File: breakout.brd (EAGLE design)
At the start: 39.4 x 50 mm, 36 parts, among them U1 ATMEGA128RFA1, U2 FT232RL

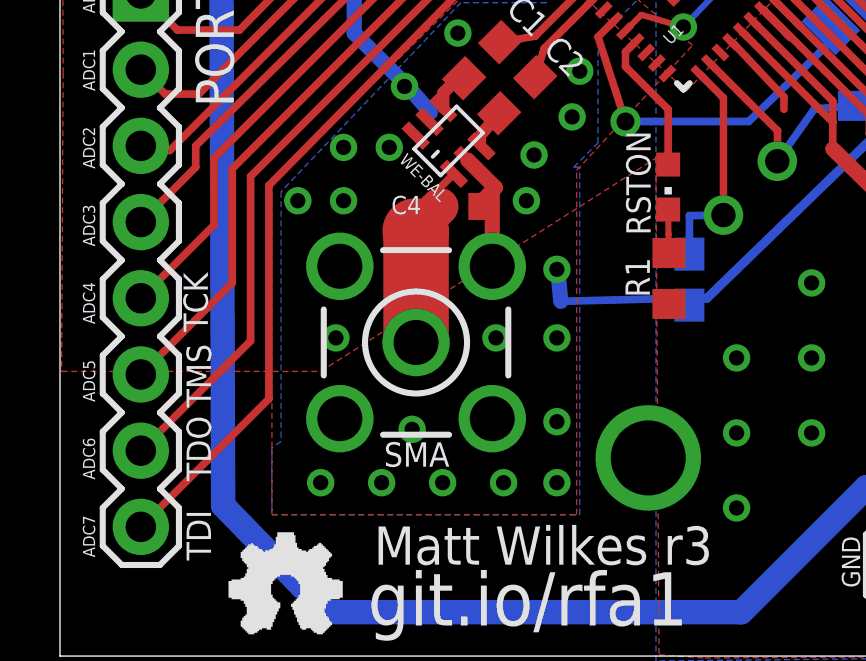
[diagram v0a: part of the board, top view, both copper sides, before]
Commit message: Switch to using a u.fl connector from SMA
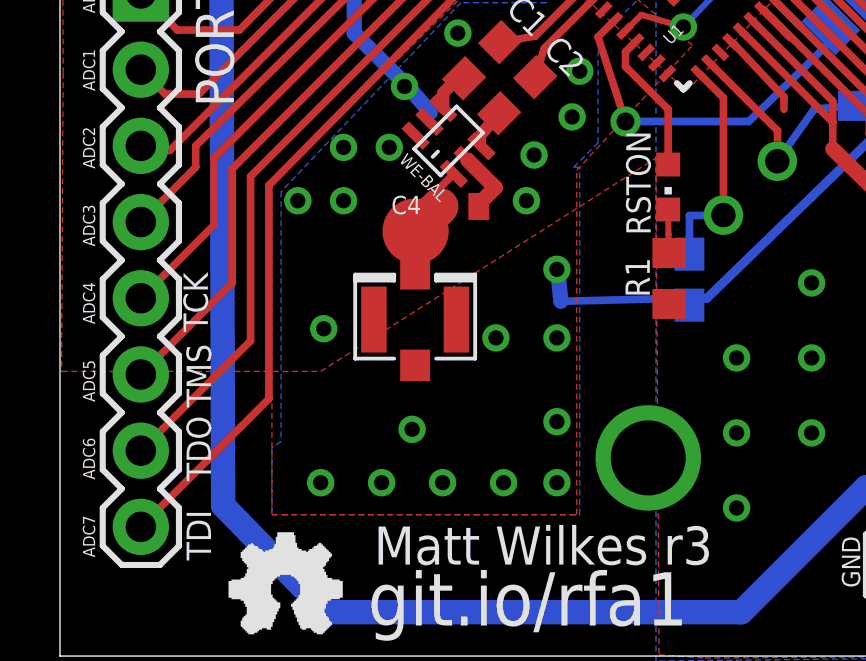
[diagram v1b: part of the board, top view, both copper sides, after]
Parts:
- removed SMA: (no value), con-coax:LTI-SASF54GT
- added U$6: U.FL, SparkFun-Connectors:U.FL
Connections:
- net GNDA: now also U$6.P$1, U$6.P$2; no longer SMA.2, SMA.3, SMA.4, SMA.5
- net SMA: now also U$6.P$3; no longer SMA.1
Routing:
- net SMA: track 6.19 -> 2.48 mm
- net GNDA: track 111.0 -> 108.5 mm
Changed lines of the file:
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@@
 <layer number="106" name="bPlate" color="7" fill="1" visible="no" active="yes"/>
 <layer number="107" name="Crop" color="7" fill="1" visible="no" active="yes"/>
+<layer number="116" name="Patch_BOT" color="9" fill="4" visible="no" active="yes"/>
 <layer number="121" name="_tsilk" color="7" fill="1" visible="no" active="yes"/>
 <layer number="122" name="_bsilk" color="7" fill="1" visible="no" active="yes"/>
@@
 <layer number="144" name="Drill_legend" color="7" fill="1" visible="no" active="yes"/>
 <layer number="151" name="HeatSink" color="7" fill="1" visible="no" active="yes"/>
+<layer number="199" name="Contour" color="7" fill="1" visible="yes" active="yes"/>
 <layer number="200" name="200bmp" color="1" fill="10" visible="no" active="yes"/>
 <layer number="201" name="201bmp" color="2" fill="10" visible="no" active="yes"/>
@@
 <layer number="220" name="220bmp" color="21" fill="1" visible="no" active="no"/>
 <layer number="221" name="221bmp" color="22" fill="1" visible="no" active="no"/>
+<layer number="222" name="222bmp" color="23" fill="1" visible="no" active="no"/>
 <layer number="223" name="223bmp" color="24" fill="1" visible="no" active="no"/>
 <layer number="224" name="224bmp" color="25" fill="1" visible="no" active="no"/>
@@
 <attribute name="VALUE" x="38.8366" y="23.4312" size="1.27" layer="27" rot="R90"/>
 </element>
-<element name="SMA" library="con-coax" package="LTI-SASF54GT" value="" x="11.8148" y="10.5156" smashed="yes" rot="R180">
-<attribute name="NAME" x="12.9324" y="7.1882" size="0.8128" layer="25" rot="R180"/>
-<attribute name="VALUE" x="14.9898" y="16.2306" size="1.27" layer="27" rot="R180"/>
-<attribute name="MF" value="" x="11.8148" y="10.5156" size="1.27" layer="27" font="fixed" rot="R180" display="off"/>
-<attribute name="MPN" value="" x="11.8148" y="10.5156" size="1.27" layer="27" font="fixed" rot="R180" display="off"/>
-<attribute name="OC_FARNELL" value="unknown" x="11.8148" y="10.5156" size="1.27" layer="27" font="fixed" rot="R180" display="off"/>
-<attribute name="OC_NEWARK" value="unknown" x="11.8148" y="10.5156" size="1.27" layer="27" font="fixed" rot="R180" display="off"/>
-</element>
 <element name="RSTON" library="led" package="CHIPLED_0603" value="" x="20.2184" y="15.6972" smashed="yes" rot="R180">
 <attribute name="NAME" x="18.8214" y="17.5768" size="0.8128" layer="25" rot="R270"/>
@@
 </element>
 <element name="C8" library="rcl" package="C0201" value="0.1µF" x="17.0688" y="30.3784" smashed="yes" rot="R225"/>
+<element name="U$6" library="SparkFun-Connectors" package="U.FL" value="U.FL" x="11.7856" y="11.2776" rot="R90"/>
 </elements>
 <signals>
@@
 <contactref element="B1" pad="NC"/>
 <contactref element="B1" pad="GNDDC"/>
-<contactref element="SMA" pad="2"/>
-<contactref element="SMA" pad="4"/>
-<contactref element="SMA" pad="3"/>
-<contactref element="SMA" pad="5"/>
 <contactref element="C4" pad="2"/>
 <wire x1="20.9544" y1="11.8624" x2="20.9268" y2="11.7608" width="0.3" layer="16"/>
@@
 <wire x1="16.6408" y1="11.8872" x2="16.5392" y2="12.9248" width="0.508" layer="16"/>
 <wire x1="14.4564" y1="15.6775" x2="13.53679375" y2="16.597203125" width="0.508" layer="1"/>
-<wire x1="13.906" y1="15.1271" x2="14.3548" y2="15.5759" width="0.508" layer="1"/>
+<wire x1="13.906" y1="15.1271" x2="14.4564" y2="15.6775" width="0.508" layer="1"/>
 <wire x1="13.906" y1="15.0492" x2="13.906" y2="15.1271" width="0.508" layer="1"/>
-<wire x1="14.3548" y1="15.5759" x2="14.4564" y2="15.6775" width="0.508" layer="1"/>
-<wire x1="14.3548" y1="15.5759" x2="14.3548" y2="13.0556" width="0.508" layer="1"/>
 <wire x1="7.7324" y1="24.2948" x2="7.7324" y2="22.646" width="0.6096" layer="16"/>
 <wire x1="7.7324" y1="22.646" x2="7.9248" y2="22.4536" width="0.6096" layer="16"/>
@@
 <via x="16.51" y="10.668" extent="1-16" drill="0.508"/>
 <via x="14.478" y="10.668" extent="1-16" drill="0.508"/>
-<via x="9.144" y="10.668" extent="1-16" drill="0.508"/>
+<via x="8.7376" y="10.9728" extent="1-16" drill="0.508"/>
 <via x="11.684" y="7.62" extent="1-16" drill="0.508"/>
 <via x="8.636" y="5.842" extent="1-16" drill="0.508"/>
@@
 <vertex x="19.5072" y="22.2504"/>
 </polygon>
+<contactref element="U$6" pad="P$2"/>
+<contactref element="U$6" pad="P$1"/>
 </signal>
 <signal name="N$10">
@@
 <signal name="SMA">
 <contactref element="C4" pad="1"/>
-<contactref element="SMA" pad="1"/>
 <contactref element="B1" pad="IN"/>
 <wire x1="12.606" y1="15.6664" x2="13.077175" y2="16.137584375" width="0.254" layer="1"/>
@@
 <wire x1="11.7856" y1="14.224" x2="11.7856" y2="14.2288" width="1.25" layer="1"/>
 <wire x1="11.8148" y1="14.224" x2="11.7856" y2="14.224" width="2.1844" layer="1"/>
-<wire x1="11.8148" y1="10.5156" x2="11.8148" y2="14.224" width="2.1844" layer="1"/>
+<contactref element="U$6" pad="P$3"/>
+<wire x1="11.7856" y1="12.8026" x2="11.7856" y2="14.2288" width="0" layer="19" extent="1-1"/>
 </signal>
 <signal name="N$12">

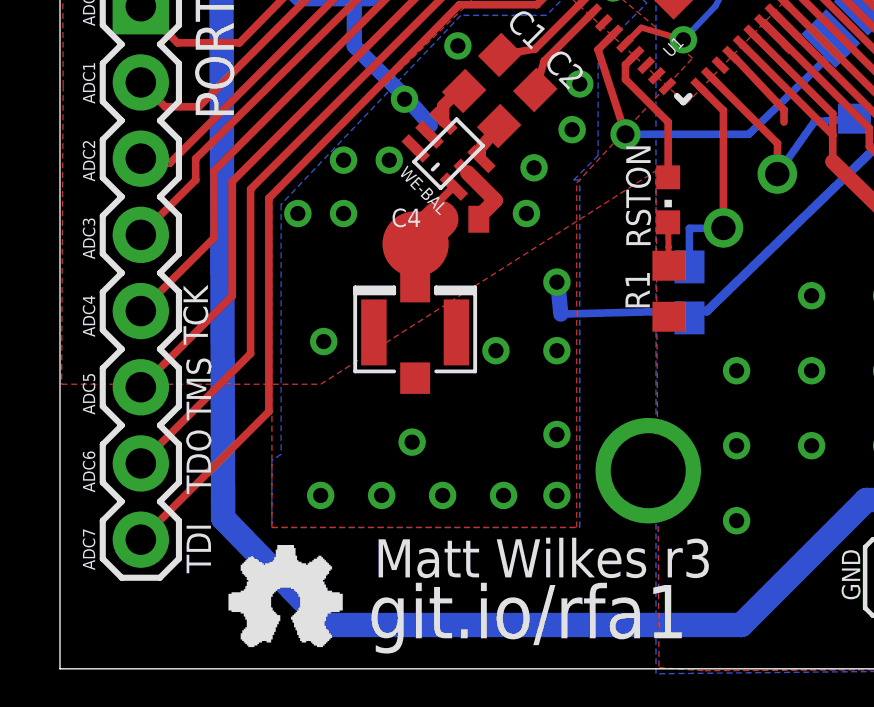
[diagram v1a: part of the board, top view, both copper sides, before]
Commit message: Reduce the size of the radio copper pour to fit u.fl
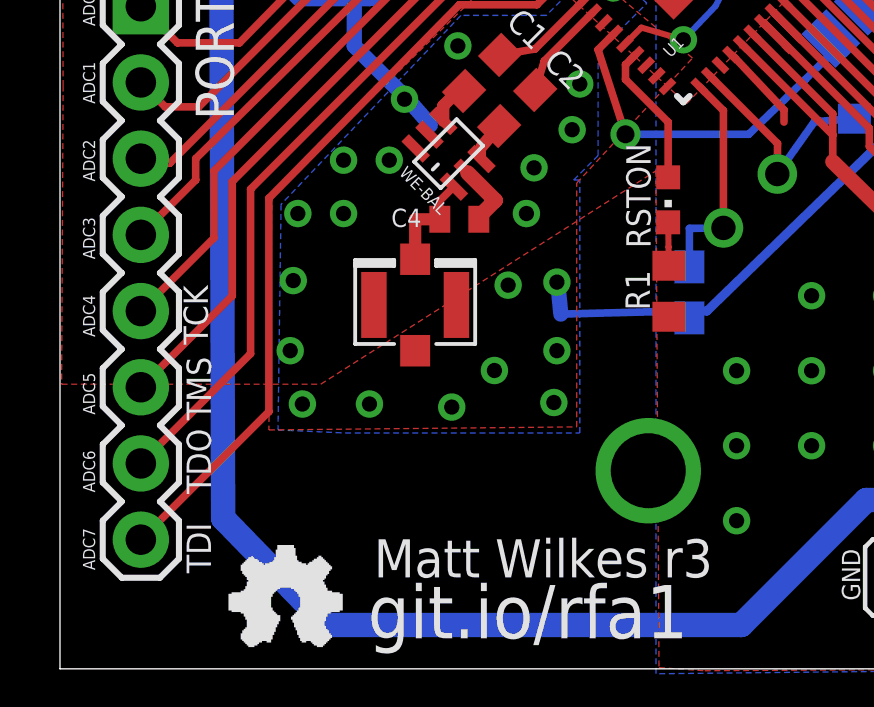
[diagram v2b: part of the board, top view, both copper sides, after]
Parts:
- moved U$6 0.91 mm to (11.8, 12.2)
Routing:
- net SMA: track 2.48 -> 3.44 mm
- net GNDA: vias 24 -> 23
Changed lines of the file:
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@@
 </element>
 <element name="C8" library="rcl" package="C0201" value="0.1µF" x="17.0688" y="30.3784" smashed="yes" rot="R225"/>
-<element name="U$6" library="SparkFun-Connectors" package="U.FL" value="U.FL" x="11.7856" y="11.2776" rot="R90"/>
+<element name="U$6" library="SparkFun-Connectors" package="U.FL" value="U.FL" x="11.7856" y="12.192" rot="R90"/>
 </elements>
 <signals>
@@
 <via x="16.51" y="12.954" extent="1-16" drill="0.508"/>
 <via x="16.51" y="10.668" extent="1-16" drill="0.508"/>
-<via x="14.478" y="10.668" extent="1-16" drill="0.508"/>
-<via x="8.7376" y="10.9728" extent="1-16" drill="0.508"/>
-<via x="11.684" y="7.62" extent="1-16" drill="0.508"/>
-<via x="8.636" y="5.842" extent="1-16" drill="0.508"/>
-<via x="10.668" y="5.842" extent="1-16" drill="0.508"/>
-<via x="12.7" y="5.842" extent="1-16" drill="0.508"/>
-<via x="14.732" y="5.842" extent="1-16" drill="0.508"/>
-<via x="16.51" y="5.842" extent="1-16" drill="0.508"/>
-<via x="16.51" y="7.874" extent="1-16" drill="0.508"/>
+<via x="16.4084" y="8.9408" extent="1-16" drill="0.508"/>
+<via x="7.7216" y="13.0048" extent="1-16" drill="0.508"/>
+<via x="7.62" y="10.668" extent="1-16" drill="0.508"/>
+<via x="8.0264" y="8.89" extent="1-16" drill="0.508"/>
+<via x="10.2616" y="8.89" extent="1-16" drill="0.508"/>
+<via x="13.0048" y="8.7884" extent="1-16" drill="0.508"/>
+<via x="14.4272" y="10.0076" extent="1-16" drill="0.508"/>
+<via x="14.8844" y="12.8524" extent="1-16" drill="0.508"/>
 <via x="18.3896" y="22.7584" extent="1-16" drill="0.508"/>
 <via x="14.9352" y="27.3304" extent="1-16" drill="0.508" shape="octagon"/>
@@
 <vertex x="15.9512" y="24.5872"/>
 <vertex x="7.0104" y="15.8496"/>
-<vertex x="7.0104" y="4.7752"/>
-<vertex x="17.1704" y="4.7752"/>
+<vertex x="6.9088" y="8.0264"/>
+<vertex x="17.1704" y="8.128"/>
 <vertex x="17.1704" y="16.256"/>
 <vertex x="21.0312" y="20.4216"/>
@@
 <vertex x="13.3096" y="21.844"/>
 <vertex x="7.3152" y="15.5448"/>
-<vertex x="7.3152" y="7.2136"/>
-<vertex x="7.0104" y="7.0104"/>
-<vertex x="7.0104" y="4.7752"/>
-<vertex x="17.272" y="4.7752"/>
+<vertex x="7.2136" y="8.0264"/>
+<vertex x="9.4488" y="7.9248"/>
+<vertex x="17.272" y="7.9248"/>
 <vertex x="17.272" y="16.3576"/>
 <vertex x="17.0688" y="16.3576"/>
@@
 <wire x1="12.606" y1="15.6664" x2="13.077175" y2="16.137584375" width="0.254" layer="1"/>
 <wire x1="12.606" y1="15.0492" x2="12.606" y2="15.6664" width="0.254" layer="1"/>
-<wire x1="11.7856" y1="14.2288" x2="12.606" y2="15.0492" width="1.25" layer="1"/>
-<wire x1="11.7856" y1="14.224" x2="11.7856" y2="14.2288" width="1.25" layer="1"/>
-<wire x1="11.8148" y1="14.224" x2="11.7856" y2="14.224" width="2.1844" layer="1"/>
 <contactref element="U$6" pad="P$3"/>
-<wire x1="11.7856" y1="12.8026" x2="11.7856" y2="14.2288" width="0" layer="19" extent="1-1"/>
+<wire x1="12.606" y1="15.0492" x2="11.7856" y2="15.0492" width="0.4064" layer="1"/>
+<wire x1="11.7856" y1="15.0492" x2="11.7856" y2="13.717" width="0.4064" layer="1"/>
 </signal>
 <signal name="N$12">
